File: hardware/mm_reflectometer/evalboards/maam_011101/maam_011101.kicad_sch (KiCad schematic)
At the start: 10 parts, among them J1 Conn_Coaxial, J2 Conn_Coaxial, U1 MAAM-011101

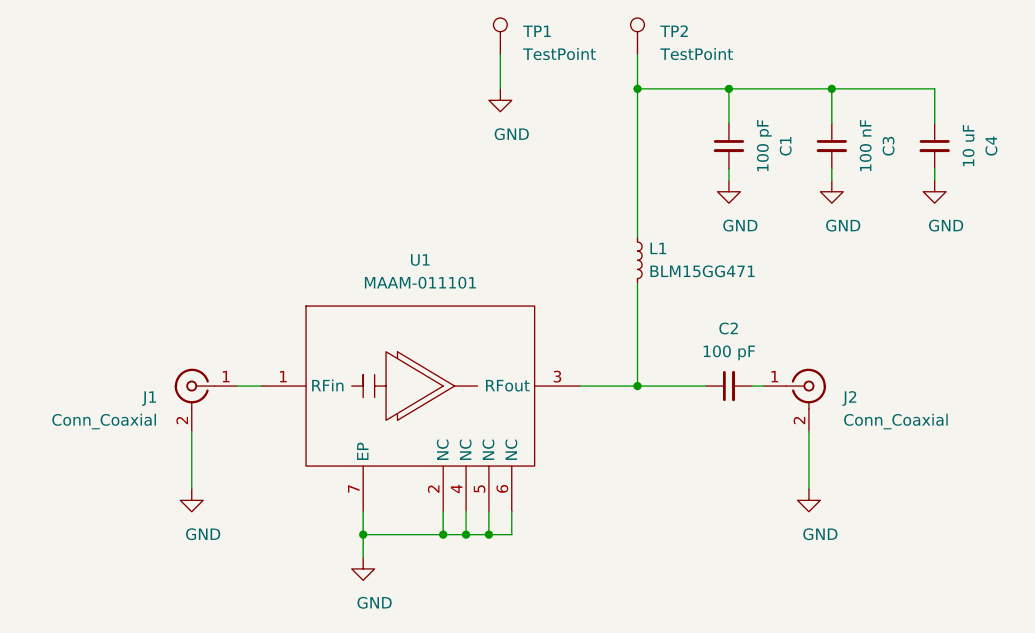
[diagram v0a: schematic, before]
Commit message: fixed maam-011101 eval board pinout, started bringup of ecp5 board
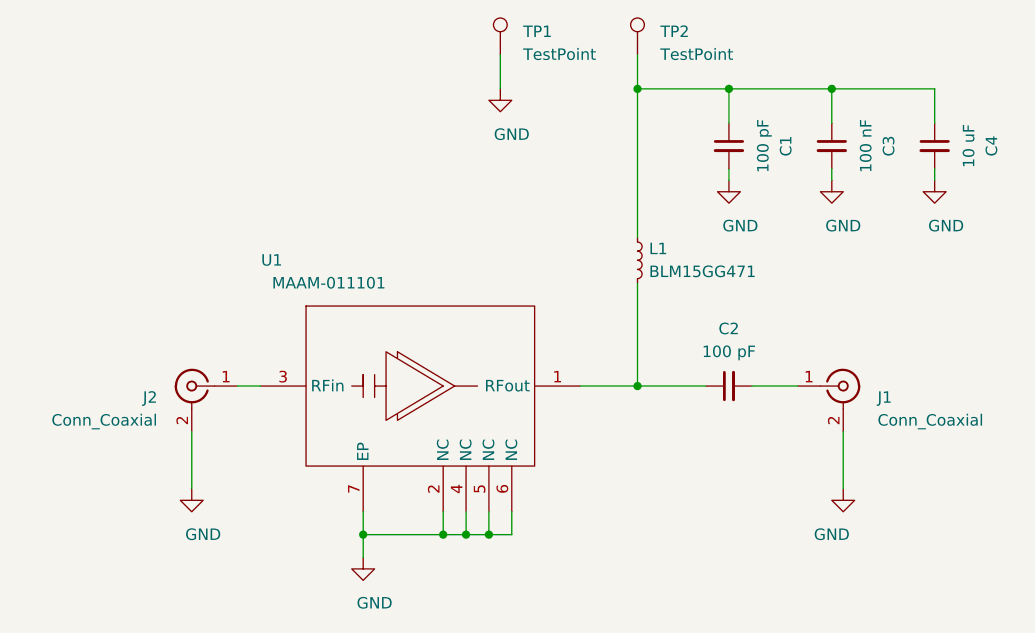
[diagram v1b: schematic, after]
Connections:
- net at C2.1, L1.2: now also U1.1 (RFout); no longer U1.3 (RFout)
- net at J1.1 (In): now also C2.2; no longer U1.1 (RFin)
- net at J2.1 (In): now also U1.3 (RFin); no longer C2.2
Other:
- moved on the sheet: J2
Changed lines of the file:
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@@
     (stroke (width 0) (type solid) (color 0 0 0 0))
   )
-  (wire (pts (xy 156.21 62.23) (xy 157.48 62.23))
-    (stroke (width 0) (type solid) (color 0 0 0 0))
-  )
-  (wire (pts (xy 162.56 67.31) (xy 162.56 73.66))
+  (wire (pts (xy 156.21 62.23) (xy 161.29 62.23))
     (stroke (width 0) (type solid) (color 0 0 0 0))
   )
@@
     (stroke (width 0) (type solid) (color 0 0 0 0))
   )
+  (wire (pts (xy 166.37 67.31) (xy 166.37 73.66))
+    (stroke (width 0) (type solid) (color 0 0 0 0))
+  )
   (wire (pts (xy 176.53 29.21) (xy 176.53 33.02))
     (stroke (width 0) (type solid) (color 0 0 0 0))
@@
   (symbol (lib_id "power:GND") (at 93.98 73.66 0) (unit 1)
     (in_bom yes) (on_board yes)
-    (property "Reference" "#PWR01" (id 0) (at 93.98 80.01 0)
+    (property "Reference" "#PWR0105" (id 0) (at 93.98 80.01 0)
       (effects (font (size 1.27 1.27)) hide)
     )
@@
     )
   )
-  (symbol (lib_id "power:GND") (at 162.56 73.66 0) (unit 1)
-    (in_bom yes) (on_board yes)
-    (property "Reference" "#PWR03" (id 0) (at 162.56 80.01 0)
-      (effects (font (size 1.27 1.27)) hide)
-    )
-    (property "Value" "GND" (id 1) (at 163.83 78.74 0))
-    (property "Footprint" "" (id 2) (at 162.56 73.66 0)
-      (effects (font (size 1.27 1.27)) hide)
-    )
-    (property "Datasheet" "" (id 3) (at 162.56 73.66 0)
-      (effects (font (size 1.27 1.27)) hide)
-    )
-  )
   (symbol (lib_id "power:GND") (at 165.1 39.37 0) (unit 1)
     (in_bom yes) (on_board yes)
@@
     )
     (property "Datasheet" "" (id 3) (at 165.1 39.37 0)
+      (effects (font (size 1.27 1.27)) hide)
+    )
+  )
+  (symbol (lib_id "power:GND") (at 166.37 73.66 0) (mirror y) (unit 1)
+    (in_bom yes) (on_board yes)
+    (property "Reference" "#PWR0106" (id 0) (at 166.37 80.01 0)
+      (effects (font (size 1.27 1.27)) hide)
+    )
+    (property "Value" "GND" (id 1) (at 165.1 78.74 0))
+    (property "Footprint" "" (id 2) (at 166.37 73.66 0)
+      (effects (font (size 1.27 1.27)) hide)
+    )
+    (property "Datasheet" "" (id 3) (at 166.37 73.66 0)
       (effects (font (size 1.27 1.27)) hide)
     )
@@
   (symbol (lib_id "Connector:Conn_Coaxial") (at 93.98 62.23 0) (mirror y) (unit 1)
     (in_bom yes) (on_board yes)
-    (property "Reference" "J1" (id 0) (at 90.17 63.5 0)
+    (property "Reference" "J2" (id 0) (at 90.17 63.5 0)
       (effects (font (size 1.27 1.27)) (justify left))
     )
@@
     )
   )
-  (symbol (lib_id "Connector:Conn_Coaxial") (at 162.56 62.23 0) (unit 1)
-    (in_bom yes) (on_board yes)
-    (property "Reference" "J2" (id 0) (at 166.37 63.5 0)
-      (effects (font (size 1.27 1.27)) (justify left))
-    )
-    (property "Value" "Conn_Coaxial" (id 1) (at 166.37 66.04 0)
-      (effects (font (size 1.27 1.27)) (justify left))
-    )
-    (property "Footprint" "jtk_rf_footprints:sw_edge_oshpark_4layer" (id 2) (at 162.56 62.23 0)
-      (effects (font (size 1.27 1.27)) hide)
-    )
-    (property "Datasheet" " ~" (id 3) (at 162.56 62.23 0)
+  (symbol (lib_id "Connector:Conn_Coaxial") (at 166.37 62.23 0) (unit 1)
+    (in_bom yes) (on_board yes)
+    (property "Reference" "J1" (id 0) (at 170.18 63.5 0)
+      (effects (font (size 1.27 1.27)) (justify left))
+    )
+    (property "Value" "Conn_Coaxial" (id 1) (at 170.18 66.04 0)
+      (effects (font (size 1.27 1.27)) (justify left))
+    )
+    (property "Footprint" "jtk_rf_footprints:sw_edge_oshpark_4layer" (id 2) (at 166.37 62.23 0)
+      (effects (font (size 1.27 1.27)) hide)
+    )
+    (property "Datasheet" " ~" (id 3) (at 166.37 62.23 0)
       (effects (font (size 1.27 1.27)) hide)
     )
@@
   (symbol (lib_id "jtk_rf:MAAM-011101") (at 118.11 62.23 0) (unit 1)
     (in_bom yes) (on_board yes)
-    (property "Reference" "U1" (id 0) (at 119.38 48.26 0))
-    (property "Value" "MAAM-011101" (id 1) (at 119.38 50.8 0))
+    (property "Reference" "U1" (id 0) (at 102.87 48.26 0))
+    (property "Value" "MAAM-011101" (id 1) (at 109.22 50.8 0))
     (property "Footprint" "jtk_rf_footprints:TDFN6" (id 2) (at 106.68 34.29 0)
       (effects (font (size 1.27 1.27)) hide)
@@
   )
   (symbol_instances
-    (path "/f0151903-ac23-4c09-8652-103a952ad6e2"
-      (reference "#PWR01") (unit 1) (value "GND") (footprint "")
-    )
     (path "/e853cee2-9307-44e4-8abb-143fc45bca6c"
       (reference "#PWR02") (unit 1) (value "GND") (footprint "")
     )
-    (path "/b907ba71-071e-4ec6-ad69-940db75afa3a"
-      (reference "#PWR03") (unit 1) (value "GND") (footprint "")
-    )
     (path "/ba5bd8f4-3a59-4338-9d7a-e72d71860d1d"
       (reference "#PWR0101") (unit 1) (value "GND") (footprint "")
@@
       (reference "#PWR0104") (unit 1) (value "GND") (footprint "")
     )
+    (path "/807b070e-60cf-4503-bf76-0c0ebb3a9f82"
+      (reference "#PWR0105") (unit 1) (value "GND") (footprint "")
+    )
+    (path "/d39a71a6-6548-40f2-855d-62a712c3a9de"
+      (reference "#PWR0106") (unit 1) (value "GND") (footprint "")
+    )
     (path "/0040d337-0b1b-4d2b-a078-d13bdee79ab3"
       (reference "C1") (unit 1) (value "100 pF") (footprint "Capacitor_SMD:C_0402_1005Metric")
@@
       (reference "C4") (unit 1) (value "10 uF") (footprint "Capacitor_SMD:C_0603_1608Metric")
     )
-    (path "/7b4bff6a-cc7c-446f-ba45-69dac277618b"
+    (path "/3b88f4f0-b2c4-41e1-ba6f-03e887708336"
       (reference "J1") (unit 1) (value "Conn_Coaxial") (footprint "jtk_rf_footprints:sw_edge_oshpark_4layer")
     )
